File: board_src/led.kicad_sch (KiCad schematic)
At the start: 17 parts, among them J29 Conn_01x08

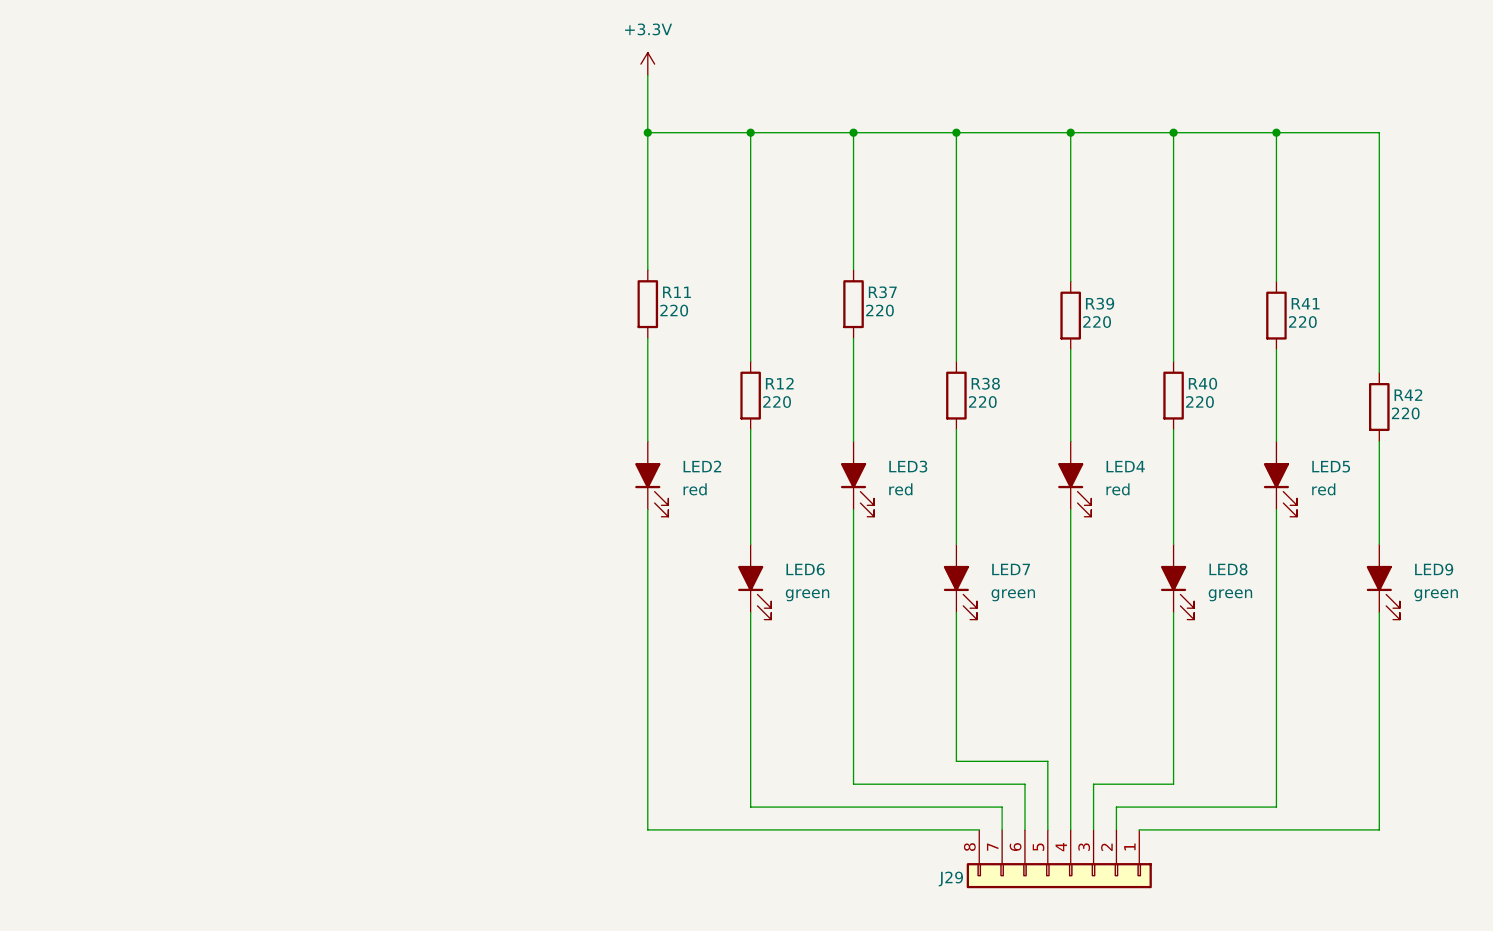
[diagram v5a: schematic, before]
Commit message: Poprawki w schematach. Rozpoczęte korekty płytki
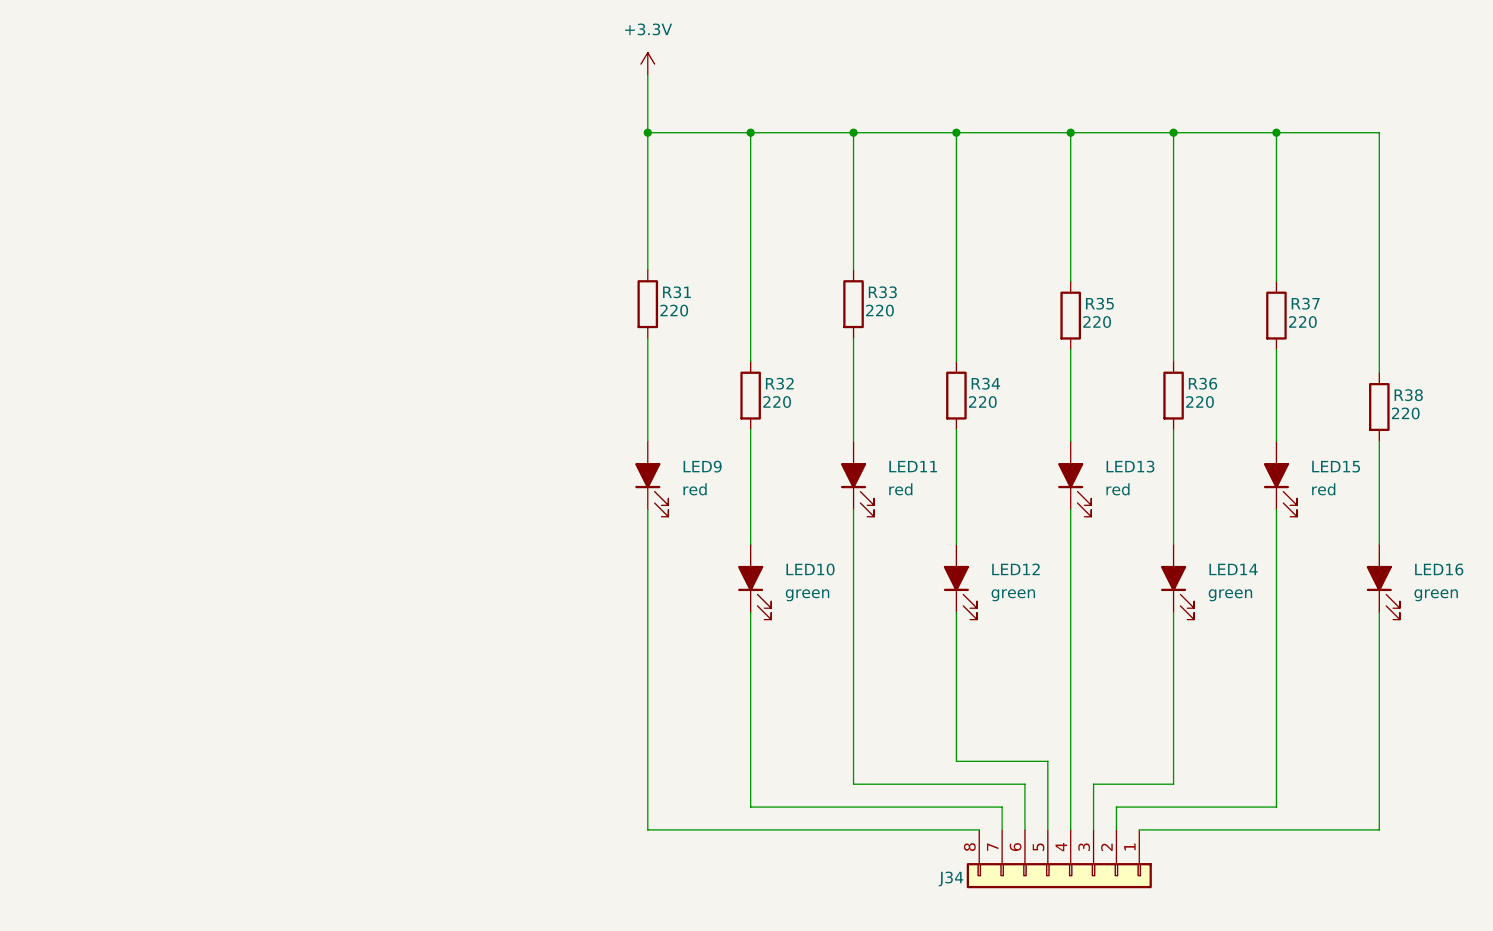
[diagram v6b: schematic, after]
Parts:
- J34: renamed from J29; footprint Connector_PinHeader_2.54mm:PinHeader_1x08_P2.54mm_Vertical -> Connector_USB:USB_C_Receptacle_HRO_TYPE-C-31-M-12
- LED10: renamed from LED6; footprint footprints:LEDC1608X100N -> LED_SMD:LED_0603_1608Metric_Pad1.05x0.95mm_HandSolder
- LED11: renamed from LED3; footprint footprints:LEDC1608X80N -> LED_SMD:LED_0603_1608Metric_Pad1.05x0.95mm_HandSolder
- LED12: renamed from LED7; footprint footprints:LEDC1608X100N -> LED_SMD:LED_0603_1608Metric_Pad1.05x0.95mm_HandSolder
- LED13: renamed from LED4; footprint footprints:LEDC1608X80N -> LED_SMD:LED_0603_1608Metric_Pad1.05x0.95mm_HandSolder
- LED14: renamed from LED8; footprint footprints:LEDC1608X100N -> LED_SMD:LED_0603_1608Metric_Pad1.05x0.95mm_HandSolder
- LED15: renamed from LED5; footprint footprints:LEDC1608X80N -> LED_SMD:LED_0603_1608Metric_Pad1.05x0.95mm_HandSolder
- LED16: renamed from LED9; footprint footprints:LEDC1608X100N -> LED_SMD:LED_0603_1608Metric_Pad1.05x0.95mm_HandSolder
- LED9: renamed from LED2; footprint footprints:LEDC1608X80N -> LED_SMD:LED_0603_1608Metric_Pad1.05x0.95mm_HandSolder
- R31: renamed from R11; footprint Resistor_SMD:R_0603_1608Metric -> Resistor_SMD:R_0603_1608Metric_Pad0.98x0.95mm_HandSolder
- R32: renamed from R12; footprint Resistor_SMD:R_0603_1608Metric -> Resistor_SMD:R_0603_1608Metric_Pad0.98x0.95mm_HandSolder
- R33: renamed from R37; footprint Resistor_SMD:R_0603_1608Metric -> Resistor_SMD:R_0603_1608Metric_Pad0.98x0.95mm_HandSolder
- R34: renamed from R38; footprint Resistor_SMD:R_0603_1608Metric -> Resistor_SMD:R_0603_1608Metric_Pad0.98x0.95mm_HandSolder
- R35: renamed from R39; footprint Resistor_SMD:R_0603_1608Metric -> Resistor_SMD:R_0603_1608Metric_Pad0.98x0.95mm_HandSolder
- R36: renamed from R40; footprint Resistor_SMD:R_0603_1608Metric -> Resistor_SMD:R_0603_1608Metric_Pad0.98x0.95mm_HandSolder
- R37: renamed from R41; footprint Resistor_SMD:R_0603_1608Metric -> Resistor_SMD:R_0603_1608Metric_Pad0.98x0.95mm_HandSolder
- R38: renamed from R42; footprint Resistor_SMD:R_0603_1608Metric -> Resistor_SMD:R_0603_1608Metric_Pad0.98x0.95mm_HandSolder
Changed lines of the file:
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@@
 		(on_board yes)
 		(dnp no)
-		(property "Reference" "J29"
+		(property "Reference" "J34"
 			(at 181.102 125.984 90)
 			(effects
@@
 			)
 		)
-		(property "Footprint" "Connector_PinHeader_2.54mm:PinHeader_1x08_P2.54mm_Vertical"
+		(property "Footprint" "Connector_USB:USB_C_Receptacle_HRO_TYPE-C-31-M-12"
 			(at 194.31 125.73 0)
 			(effects
@@
 			(project "board"
 				(path "/772e9f49-cfcf-4cf6-843d-0684684f2d4b/b28b7f90-4697-49e2-9c2e-20213e860225"
-					(reference "J29")
+					(reference "J34")
 					(unit 1)
 				)
@@
 		(on_board yes)
 		(dnp no)
-		(property "Reference" "R42"
+		(property "Reference" "R38"
 			(at 230.124 72.39 0)
 			(effects
@@
 			)
 		)
-		(property "Footprint" "Resistor_SMD:R_0603_1608Metric"
+		(property "Footprint" "Resistor_SMD:R_0603_1608Metric_Pad0.98x0.95mm_HandSolder"
 			(at 226.822 73.66 90)
 			(effects
@@
 			(project "board"
 				(path "/772e9f49-cfcf-4cf6-843d-0684684f2d4b/b28b7f90-4697-49e2-9c2e-20213e860225"
-					(reference "R42")
+					(reference "R38")
 					(unit 1)
 				)
@@
 		(on_board yes)
 		(dnp no)
-		(property "Reference" "R40"
+		(property "Reference" "R36"
 			(at 207.264 71.12 0)
 			(effects
@@
 			)
 		)
-		(property "Footprint" "Resistor_SMD:R_0603_1608Metric"
+		(property "Footprint" "Resistor_SMD:R_0603_1608Metric_Pad0.98x0.95mm_HandSolder"
 			(at 203.962 72.39 90)
 			(effects
@@
 			(project "board"
 				(path "/772e9f49-cfcf-4cf6-843d-0684684f2d4b/b28b7f90-4697-49e2-9c2e-20213e860225"
-					(reference "R40")
+					(reference "R36")
 					(unit 1)
 				)
@@
 		(dnp no)
 		(fields_autoplaced yes)
-		(property "Reference" "LED9"
+		(property "Reference" "LED16"
 			(at 232.41 91.7574 90)
 			(effects
@@
 			)
 		)
-		(property "Footprint" "footprints:LEDC1608X100N"
+		(property "Footprint" "LED_SMD:LED_0603_1608Metric_Pad1.05x0.95mm_HandSolder"
 			(at 228.6 92.71 0)
 			(effects
@@
 			(project "board"
 				(path "/772e9f49-cfcf-4cf6-843d-0684684f2d4b/b28b7f90-4697-49e2-9c2e-20213e860225"
-					(reference "LED9")
+					(reference "LED16")
 					(unit 1)
 				)
@@
 		(dnp no)
 		(fields_autoplaced yes)
-		(property "Reference" "LED2"
+		(property "Reference" "LED9"
 			(at 151.13 80.3274 90)
 			(effects
@@
 			)
 		)
-		(property "Footprint" "footprints:LEDC1608X80N"
+		(property "Footprint" "LED_SMD:LED_0603_1608Metric_Pad1.05x0.95mm_HandSolder"
 			(at 147.32 81.28 0)
 			(effects
@@
 			(project ""
 				(path "/772e9f49-cfcf-4cf6-843d-0684684f2d4b/b28b7f90-4697-49e2-9c2e-20213e860225"
-					(reference "LED2")
+					(reference "LED9")
 					(unit 1)
 				)
@@
 		(dnp no)
 		(fields_autoplaced yes)
-		(property "Reference" "LED4"
+		(property "Reference" "LED13"
 			(at 198.12 80.3274 90)
 			(effects
@@
 			)
 		)
-		(property "Footprint" "footprints:LEDC1608X80N"
+		(property "Footprint" "LED_SMD:LED_0603_1608Metric_Pad1.05x0.95mm_HandSolder"
 			(at 194.31 81.28 0)
 			(effects
@@
 			(project "board"
 				(path "/772e9f49-cfcf-4cf6-843d-0684684f2d4b/b28b7f90-4697-49e2-9c2e-20213e860225"
-					(reference "LED4")
+					(reference "LED13")
 					(unit 1)
 				)
@@
 		(on_board yes)
 		(dnp no)
-		(property "Reference" "R37"
+		(property "Reference" "R33"
 			(at 171.704 60.96 0)
 			(effects
@@
 			)
 		)
-		(property "Footprint" "Resistor_SMD:R_0603_1608Metric"
+		(property "Footprint" "Resistor_SMD:R_0603_1608Metric_Pad0.98x0.95mm_HandSolder"
 			(at 168.402 62.23 90)
 			(effects
@@
 			(project "board"
 				(path "/772e9f49-cfcf-4cf6-843d-0684684f2d4b/b28b7f90-4697-49e2-9c2e-20213e860225"
-					(reference "R37")
+					(reference "R33")
 					(unit 1)
 				)
@@
 		(on_board yes)
 		(dnp no)
-		(property "Reference" "R11"
+		(property "Reference" "R31"
 			(at 148.844 60.96 0)
 			(effects
@@
 			)
 		)
-		(property "Footprint" "Resistor_SMD:R_0603_1608Metric"
+		(property "Footprint" "Resistor_SMD:R_0603_1608Metric_Pad0.98x0.95mm_HandSolder"
 			(at 145.542 62.23 90)
 			(effects
@@
 			(project "board"
 				(path "/772e9f49-cfcf-4cf6-843d-0684684f2d4b/b28b7f90-4697-49e2-9c2e-20213e860225"
-					(reference "R11")
+					(reference "R31")
 					(unit 1)
 				)
@@
 		(on_board yes)
 		(dnp no)
-		(property "Reference" "R39"
+		(property "Reference" "R35"
 			(at 195.834 62.23 0)
 			(effects
@@
 			)
 		)
-		(property "Footprint" "Resistor_SMD:R_0603_1608Metric"
+		(property "Footprint" "Resistor_SMD:R_0603_1608Metric_Pad0.98x0.95mm_HandSolder"
 			(at 192.532 63.5 90)
 			(effects
@@
 			(project "board"
 				(path "/772e9f49-cfcf-4cf6-843d-0684684f2d4b/b28b7f90-4697-49e2-9c2e-20213e860225"
-					(reference "R39")
+					(reference "R35")
 					(unit 1)
 				)
@@
 		(dnp no)
 		(fields_autoplaced yes)
-		(property "Reference" "#PWR023"
+		(property "Reference" "#PWR068"
 			(at 147.32 40.64 0)
 			(effects
@@
 			(project ""
 				(path "/772e9f49-cfcf-4cf6-843d-0684684f2d4b/b28b7f90-4697-49e2-9c2e-20213e860225"
-					(reference "#PWR023")
+					(reference "#PWR068")
 					(unit 1)
 				)
@@
 		(on_board yes)
 		(dnp no)
-		(property "Reference" "R38"
+		(property "Reference" "R34"
 			(at 183.134 71.12 0)
 			(effects
@@
 			)
 		)
-		(property "Footprint" "Resistor_SMD:R_0603_1608Metric"
+		(property "Footprint" "Resistor_SMD:R_0603_1608Metric_Pad0.98x0.95mm_HandSolder"
 			(at 179.832 72.39 90)
 			(effects
@@
 			(project "board"
 				(path "/772e9f49-cfcf-4cf6-843d-0684684f2d4b/b28b7f90-4697-49e2-9c2e-20213e860225"
-					(reference "R38")
+					(reference "R34")
 					(unit 1)
 				)
@@
 		(dnp no)
 		(fields_autoplaced yes)
-		(property "Reference" "LED7"
+		(property "Reference" "LED12"
 			(at 185.42 91.7574 90)
 			(effects
@@
 			)
 		)
-		(property "Footprint" "footprints:LEDC1608X100N"
+		(property "Footprint" "LED_SMD:LED_0603_1608Metric_Pad1.05x0.95mm_HandSolder"
 			(at 181.61 92.71 0)
 			(effects
@@
 			(project "board"
 				(path "/772e9f49-cfcf-4cf6-843d-0684684f2d4b/b28b7f90-4697-49e2-9c2e-20213e860225"
-					(reference "LED7")
+					(reference "LED12")
 					(unit 1)
 				)
@@
 		(dnp no)
 		(fields_autoplaced yes)
-		(property "Reference" "LED8"
+		(property "Reference" "LED14"
 			(at 209.55 91.7574 90)
 			(effects
@@
 			)
 		)
-		(property "Footprint" "footprints:LEDC1608X100N"
+		(property "Footprint" "LED_SMD:LED_0603_1608Metric_Pad1.05x0.95mm_HandSolder"
 			(at 205.74 92.71 0)
 			(effects
@@
 			(project "board"
 				(path "/772e9f49-cfcf-4cf6-843d-0684684f2d4b/b28b7f90-4697-49e2-9c2e-20213e860225"
-					(reference "LED8")
+					(reference "LED14")
 					(unit 1)
 				)
@@
 		(on_board yes)
 		(dnp no)
-		(property "Reference" "R41"
+		(property "Reference" "R37"
 			(at 218.694 62.23 0)
 			(effects
@@
 			)
 		)
-		(property "Footprint" "Resistor_SMD:R_0603_1608Metric"
+		(property "Footprint" "Resistor_SMD:R_0603_1608Metric_Pad0.98x0.95mm_HandSolder"
 			(at 215.392 63.5 90)
 			(effects
@@
 			(project "board"
 				(path "/772e9f49-cfcf-4cf6-843d-0684684f2d4b/b28b7f90-4697-49e2-9c2e-20213e860225"
-					(reference "R41")
+					(reference "R37")
 					(unit 1)
 				)
@@
 		(dnp no)
 		(fields_autoplaced yes)
-		(property "Reference" "LED5"
+		(property "Reference" "LED15"
 			(at 220.98 80.3274 90)
 			(effects
@@
 			)
 		)
-		(property "Footprint" "footprints:LEDC1608X80N"
+		(property "Footprint" "LED_SMD:LED_0603_1608Metric_Pad1.05x0.95mm_HandSolder"
 			(at 217.17 81.28 0)
 			(effects
@@
 			(project "board"
 				(path "/772e9f49-cfcf-4cf6-843d-0684684f2d4b/b28b7f90-4697-49e2-9c2e-20213e860225"
-					(reference "LED5")
+					(reference "LED15")
 					(unit 1)
 				)
@@
 		(dnp no)
 		(fields_autoplaced yes)
-		(property "Reference" "LED6"
+		(property "Reference" "LED10"
 			(at 162.56 91.7574 90)
 			(effects
@@
 			)
 		)
-		(property "Footprint" "footprints:LEDC1608X100N"
+		(property "Footprint" "LED_SMD:LED_0603_1608Metric_Pad1.05x0.95mm_HandSolder"
 			(at 158.75 92.71 0)
 			(effects
@@
 			(project ""
 				(path "/772e9f49-cfcf-4cf6-843d-0684684f2d4b/b28b7f90-4697-49e2-9c2e-20213e860225"
-					(reference "LED6")
+					(reference "LED10")
 					(unit 1)
 				)
@@
 		(on_board yes)
 		(dnp no)
-		(property "Reference" "R12"
+		(property "Reference" "R32"
 			(at 160.274 71.12 0)
 			(effects
@@
 			)
 		)
-		(property "Footprint" "Resistor_SMD:R_0603_1608Metric"
+		(property "Footprint" "Resistor_SMD:R_0603_1608Metric_Pad0.98x0.95mm_HandSolder"
 			(at 156.972 72.39 90)
 			(effects
@@
 			(project "board"
 				(path "/772e9f49-cfcf-4cf6-843d-0684684f2d4b/b28b7f90-4697-49e2-9c2e-20213e860225"
-					(reference "R12")
+					(reference "R32")
 					(unit 1)
 				)
@@
 		(dnp no)
 		(fields_autoplaced yes)
-		(property "Reference" "LED3"
+		(property "Reference" "LED11"
 			(at 173.99 80.3274 90)
 			(effects
@@
 			)
 		)
-		(property "Footprint" "footprints:LEDC1608X80N"
+		(property "Footprint" "LED_SMD:LED_0603_1608Metric_Pad1.05x0.95mm_HandSolder"
 			(at 170.18 81.28 0)
 			(effects
@@
 			(project "board"
 				(path "/772e9f49-cfcf-4cf6-843d-0684684f2d4b/b28b7f90-4697-49e2-9c2e-20213e860225"
-					(reference "LED3")
-					(unit 1)
-				)
+					(reference "LED11")
+					(unit 1)
+				)

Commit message: Wprowadzono usprawnienia i poprawki. Wersja ostateczna, wysłana do JLCPCB.
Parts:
- J34: footprint Connector_USB:USB_C_Receptacle_HRO_TYPE-C-31-M-12 -> Connector_PinHeader_2.54mm:PinHeader_1x08_P2.54mm_Vertical
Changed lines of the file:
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@@
 			)
 		)
-		(property "Footprint" "Connector_USB:USB_C_Receptacle_HRO_TYPE-C-31-M-12"
+		(property "Footprint" "Connector_PinHeader_2.54mm:PinHeader_1x08_P2.54mm_Vertical"
 			(at 194.31 125.73 0)
 			(effects
